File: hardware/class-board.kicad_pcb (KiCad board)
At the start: 4 copper layers, 180 x 100 mm, 334 parts, among them J1 DevKit J1 (left row), J10 C2937625_-_Conn_01x03, J11 C2937625_-_Conn_01x03, J12 C2937625_-_Conn_01x03, J13 C492401-PZ254V-11-02P, J14 C2937625_-_Conn_01x03, J15 C2937625_-_Conn_01x03, J2 DevKit J3 (right row), J201 USB-C 16P, J202 DC005-T20, J3 C2937625_-_Conn_01x03, J4 Qwiic, J5 Expansion 2x10, J6 Panel link 2x20 female, J7 Panel link 2x20 female, J8 Panel link 2x20 female, J9 C2937625_-_Conn_01x03, J901 KF301-5.0-2P, J903 KF301-5.0-2P, J905 KF301-5.0-3P, Q901 AOD4185, Q904 AOD4184A, U101 ADS8688IDBTR, U201 LM66100DCKR, U202 LM66100DCKR, U203 78L05G-AB3-R, U204 AMS1117-3.3, U301 DAC8563SDGSR, U302 74HCT125PW, U303 OPA2192IDR, U501 SN74AHCT541PWR, U502 74HCT125PW, U503 SN74LVC1T45DBVR, U505 TCA9535PWR, U701 SI5351A-B-GT, U702 74HC74D,653, U703 OPA1656IDR, U704 DG419DY-T1-E3, U705 OPA1612AIDR, U706 OPA1612AIDR, U801 AD9834BRUZ, U802 OPA564AIDWPR, U901 TS5A23157DGSR, U902 TS5A23157DGSR, U903 DRV8871DDAR, U904 UCC27517DBVR, Y701 25 MHz

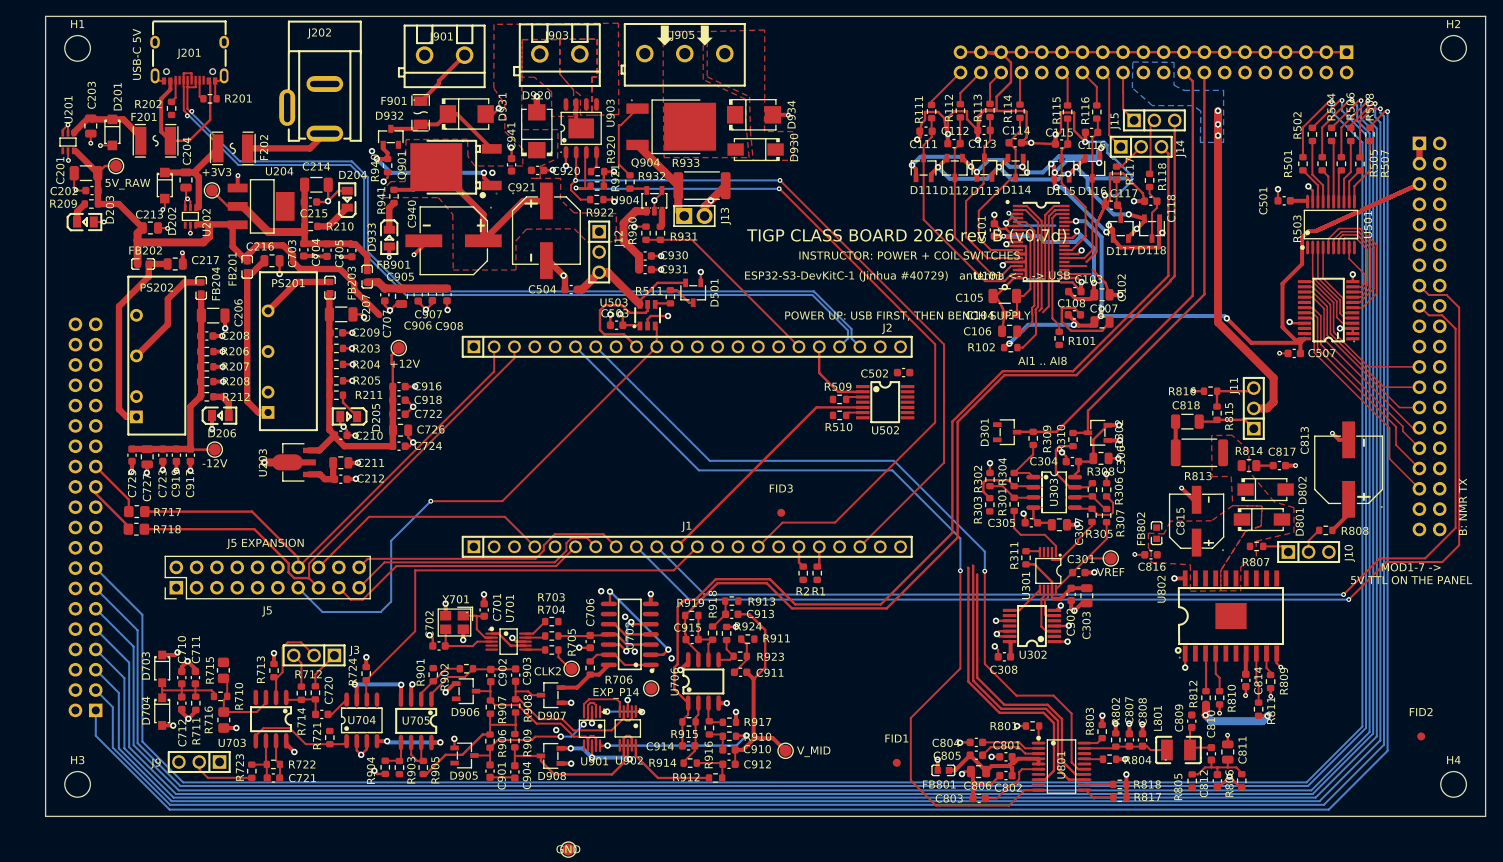
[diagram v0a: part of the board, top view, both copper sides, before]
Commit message: Main board: five copper zones restored (missing from the 2026-09-24 save), student A's area-A routing accepted (26 items; 157 unconnected); Decision #70: three students on the boards (A Renqian, B Yi-Tsai, C instructor, D Lihdong) in both sections READMEs; sections re-split
Co-Authored-By: Claude Fable 5.1 <noreply@anthropic.com>
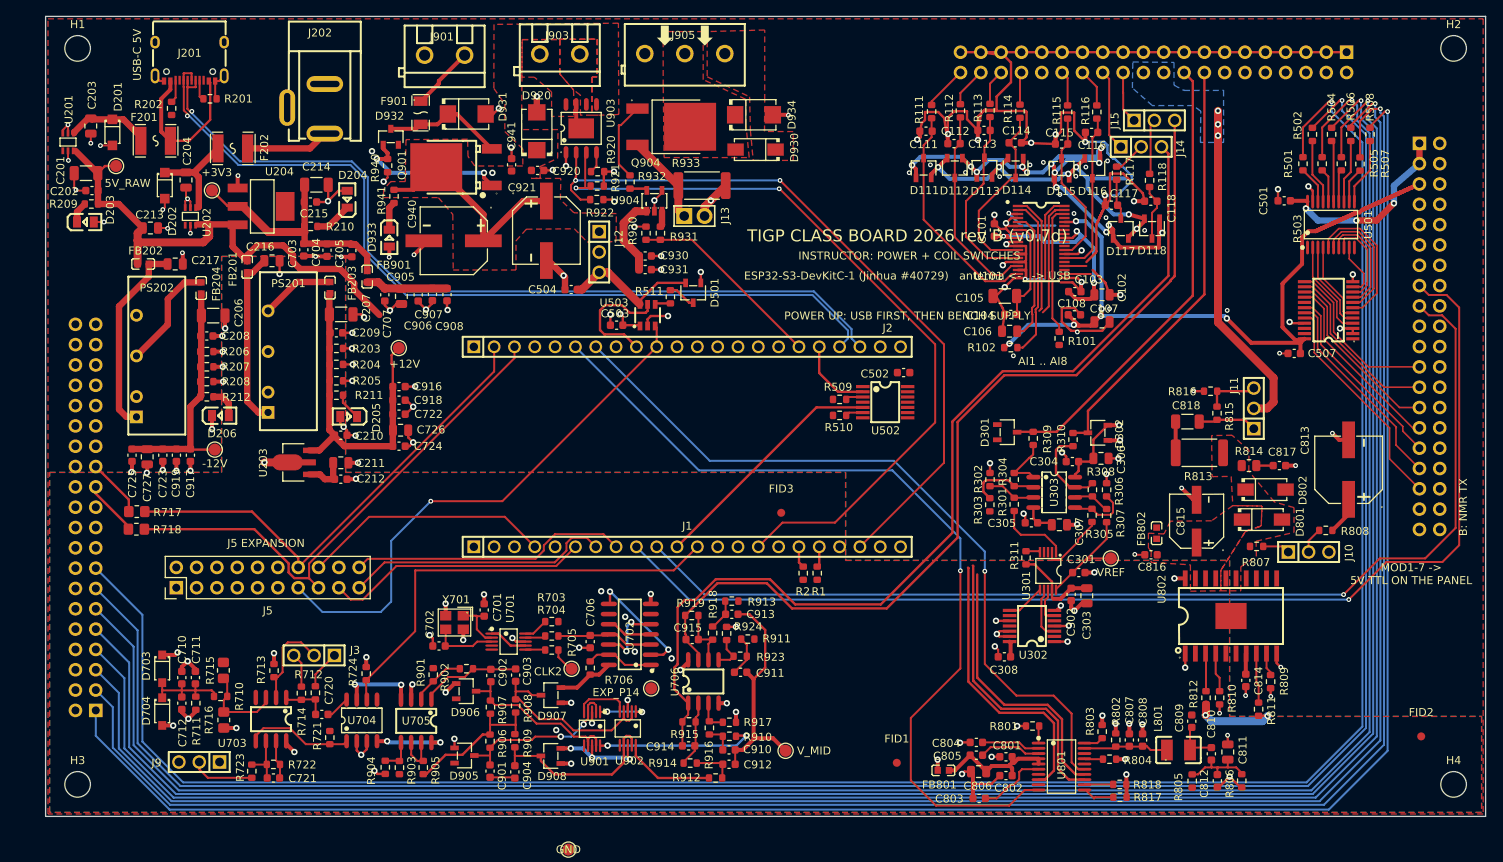
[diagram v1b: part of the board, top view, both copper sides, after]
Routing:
- net +5V_RAW: track 89.1 -> 108.1 mm, vias 0 -> 3
- net GND: vias 69 -> 86
- added copper zone on B.Cu, net AGND
- added copper zone on F.Cu, net AGND
- added copper zone on F.Cu, net GND
- added copper zone on In1.Cu, net GND
- added copper zone on In2.Cu, net GND

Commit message: hardware: instructor's masters of 2026-09-25 04:25 (main board) and 2026-09-24 22:43 (panel + schematic)
Co-Authored-By: Claude Fable 5.1 <noreply@anthropic.com>
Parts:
- moved J5 90.1 mm to (-62.8, 43.4)
- moved R717 90.1 mm to (-67.7, 33.8)
- moved R718 90.1 mm to (-67.8, 36.0)
- moved TP203 21.7 mm to (44.0, 78.1)
- moved C216 19.9 mm to (32.4, 65.0)
- moved C217 19.7 mm to (16.3, 65.7)
- moved FB203 19.4 mm to (37.3, 68.2)
- moved C207 19.2 mm to (38.5, 71.4)
- moved C209 19.2 mm to (36.9, 73.7)
- moved C210 19.2 mm to (37.5, 86.5)
- moved C707 19.2 mm to (43.0, 69.0)
- moved C722 19.2 mm to (44.7, 83.9)
- moved C723 19.2 mm to (15.2, 89.0)
- moved C724 19.2 mm to (44.7, 87.9)
- moved C725 19.2 mm to (11.4, 89.0)
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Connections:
- J6 pad 1: AGND -> GND
- J6 pad 10: unconnected-(J6-Pad10) -> /b1_inputs/TX
- J6 pad 11: AGND -> GND
- J6 pad 12: /b1_inputs/AUX -> /b1_inputs/TX
- J6 pad 13: AGND -> unconnected-(J6-Pad13)
- J6 pad 20: /b1_inputs/TX -> /b1_inputs/AUX
- J6 pad 22: /b1_inputs/TX -> /b1_inputs/RX
- J6 pad 3: AGND -> GND
- J6 pad 32: /b1_inputs/RX -> unconnected-(J6-Pad32)
- J6 pad 5: AGND -> GND
- J6 pad 7: AGND -> GND
- J6 pad 9: AGND -> GND
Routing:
- net /b1_inputs/AUX: track 12.2 -> 222.1 mm
- net /b1_inputs/RX: track 0.00 -> 209.7 mm
- net +5V_RAW: track 108.1 -> 291.1 mm, vias 3 -> 9
- net I2C_SDA: track 0.00 -> 155.9 mm, vias 0 -> 2
- net I2C_SCL: track 0.00 -> 150.3 mm, vias 0 -> 2
- net -12V: track 115.1 -> 259.0 mm, vias 17 -> 15
- net AGND: track 312.6 -> 174.7 mm, vias 87 -> 88
- net +VEXT: track 28.0 -> 161.4 mm, vias 0 -> 4
- net +3V3A: track 35.9 -> 146.2 mm, vias 3 -> 12
- net +5VA: track 44.9 -> 150.0 mm, vias 3 -> 6
- net +12V: track 114.1 -> 218.3 mm
- net /base_mcu/TX_EN: track 4.90 -> 101.4 mm, vias 0 -> 2
- net +3V3: track 147.6 -> 236.3 mm, vias 10 -> 11
- net /nmr_tx/+VEXT_TX: track 0.00 -> 54.3 mm
- net /b1_inputs/CS_ADC: track 10.8 -> 64.4 mm, vias 0 -> 2
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- added copper zone on F.Cu, net +VCOIL
- added copper zone on F.Cu, net /b1_inputs/TX
- added copper zone on F.Cu, net /nmr_rx/IF_QN
- added copper zone on In1.Cu, net AGND
- added copper zone on In2.Cu, net AGND
- added copper zone on B.Cu, net GND
- removed copper zone on F.Cu, net (none)
- removed copper zone on B.Cu, net /b1_inputs/TX
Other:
- board text added: "ESP32-S3-DevKitC-1 (Jinhua #40729)"
- board text removed: "ESP32-S3-DevKitC-1 (Jinhua #40729) antenna <- -> USB"
- board text removed: "INSTRUCTOR: POWER + COIL SWITCHES"
- board text removed: "J7 PANEL LINK pin 1 ->"
- board text removed: "J8 PANEL LINK pin 1 ->"

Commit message: hardware: the instructor's main-board save of 2026-09-30 18:24 (sheets and DC jack footprint from 2026-09-27)
Co-Authored-By: Claude Fable 5.1 <noreply@anthropic.com>
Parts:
- removed J4: Qwiic, class_board:CONN-SMD_4P-P1.00_XY-SM04B-SRSS-TB
- removed J5: Expansion 2x10, Connector_PinHeader_2.54mm:PinHeader_2x10_P2.54mm_Vertical
- removed R701, R702: 4.7k, Resistor_SMD:R_0603_1608Metric
- moved TP101 121.7 mm to (137.3, 47.5)
- moved TP2 110.3 mm to (173.2, 95.8)
- moved TP4 104.5 mm to (8.15, 44.0)
- moved R717 87.4 mm to (18.4, 48.9)
- moved TP3 87.0 mm to (42.9, 47.2)
- moved R718 86.8 mm to (18.4, 46.8)
- moved R4 80.7 mm to (63.6, 52.8), turned to -90 degrees
- moved R3 78.0 mm to (61.2, 52.6), turned to -90 degrees
- moved TP205 47.9 mm to (118.8, 80.8)
- moved R719 46.3 mm to (131.3, 99.7)
- moved TP1 45.3 mm to (58.6, 84.8)
- moved TP206 42.1 mm to (129.5, 94.5)
- moved C816 1.50 mm to (139.0, 83.5), turned to -90 degrees
- moved C802 0.65 mm to (120.0, 109.2)
- moved U903 0.36 mm to (66.8, 29.4)
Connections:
- net /base_mcu/TRIG_IO renamed /b5_dio_trig/TRIG_IO
- J1 pad 4: /base_mcu/GPIO4 -> unconnected-(J1-IO4-Pad4)
- J1 pad 6: /base_mcu/GPIO6 -> unconnected-(J1-IO6-Pad6)
- J1 pad 7: /base_mcu/GPIO7 -> unconnected-(J1-IO7-Pad7)
- J1 pad 8: /base_mcu/GPIO15 -> unconnected-(J1-IO15-Pad8)
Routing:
- net +3V3: track 236.3 -> 524.8 mm, vias 11 -> 19
- net /b5_dio_trig/EXP_P14: track 11.4 -> 147.1 mm, vias 0 -> 4
- net +12V: track 218.3 -> 349.9 mm, vias 11 -> 13
- net /b5_dio_trig/FASTTTL1: track 0.00 -> 96.0 mm, vias 0 -> 1
- net /b5_dio_trig/FASTTTL2: track 0.00 -> 95.8 mm, vias 0 -> 1
- net -12V: track 259.0 -> 353.7 mm, vias 15 -> 17
- net /b5_dio_trig/TRIG_5V: track 3.50 -> 88.4 mm, vias 0 -> 1
- net I2C_SCL: track 150.3 -> 212.5 mm, vias 2 -> 3
- net I2C_SDA: track 155.9 -> 215.3 mm, vias 2 -> 3
- net +5V_RAW: track 291.1 -> 348.6 mm, vias 9 -> 8
- net /nmr_rx/CLK0_MCLK: track 21.5 -> 77.1 mm, vias 0 -> 2
- net +5VA: track 150.0 -> 200.6 mm, vias 6 -> 7
- net SPI_MOSI: track 87.6 -> 134.4 mm, vias 0 -> 3
- net /b5_dio_trig/LED_ACT: track 1.21 -> 44.6 mm, vias 0 -> 1
- net SPI_SCLK: track 84.4 -> 126.4 mm, vias 0 -> 3
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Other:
- board text added: "AGND-GND Bridge"
- board text removed: "A: NMR RECEIVER"
- board text removed: "J5 EXPANSION"
- board text removed: "J6 PANEL LINK pin 1 ->"
